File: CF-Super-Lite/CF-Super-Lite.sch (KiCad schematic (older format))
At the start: 11 parts, among them J1 Bus_ISA_8bit, J2 ATA_CONNECTOR, SW1 DIP Switch x3 or x4, U1 BIOS FLASH, U2 74HCT245, U3 GAL16V8

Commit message: Add power for CF adapter to Template and CF-Super-Lite.
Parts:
- removed J2: ATA_CONNECTOR, Connector_PinSocket_2.54mm:PinSocket_2x20_P2.54mm_Vertical, symbol 00Common:IDE_CONNECTOR
- added J1: IDE_CONNECTOR, Connector_PinSocket_2.54mm:PinSocket_2x20_P2.54mm_Vertical, symbol 00Common:IDE_CONNECTOR
- added J2: CF Adapter Power, Connector_PinHeader_2.54mm:PinHeader_1x02_P2.54mm_Vertical, symbol Connector_Generic:Conn_01x02
- renumbered J1 to J3
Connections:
- net A0: now also J1.35 (A0)
- net A1: now also J1.33 (A1)
- net A2: now also J1.36 (A2)
- net D0_BUF: now also J1.17 (D0)
- net D1_BUF: now also J1.15 (D1)
- net D2_BUF: now also J1.13 (D2)
- net D3_BUF: now also J1.11 (D3)
- net D4_BUF: now also J1.9 (D4)
- net D5_BUF: now also J1.7 (D5)
- net D6_BUF: now also J1.5 (D6)
- net D7_BUF: now also J1.3 (D7)
- net GND: now also J1.19 (GND), J1.2 (GND), J1.22 (GND), J1.24 (GND), J1.26 (GND), J1.28 (CSEL), J1.30 (GND), J1.40 (GND), J2.2 (Pin_2)
- net VCC: now also J2.1 (Pin_1)
- net ~CS0~_ATA: now also J1.37 (~CS1)
- net ~CS1~_ATA: now also J1.38 (~CS3)
- net ~IOR: now also J1.25 (~IOR)
- net ~IOW: now also J1.23 (~IOW)
- net ~RESET: now also J1.1 (~RESET)
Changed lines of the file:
@@
 	1600 3800 1100 3800
 $Comp
-L 00Common:Bus_ISA_8bit J1
+L 00Common:Bus_ISA_8bit J3
 U 1 1 6039F90B
 P 2100 2600
-F 0 "J1" H 2100 4367 50  0000 C CNN
+F 0 "J3" H 2100 4367 50  0000 C CNN
 F 1 "Bus_ISA_8bit" H 2100 4276 50  0000 C CNN
 F 2 "00Custom:BUS_XT" H 2100 2600 50  0001 C CNN
@@
 Wire Wire Line
 	1050 1400 1600 1400
-$Comp
-L 00Common:IDE_CONNECTOR J2
-U 1 1 60482C53
-P 9250 950
-F 0 "J2" H 9250 1115 50  0000 C CNN
-F 1 "ATA_CONNECTOR" H 9250 1024 50  0000 C CNN
-F 2 "Connector_PinSocket_2.54mm:PinSocket_2x20_P2.54mm_Vertical" H 9250 950 50  0001 C CNN
-F 3 "" H 9250 950 50  0001 C CNN
-	1    9250 950
-	1    0    0    -1
-$EndComp
 Text Notes 550  7700 0    50   ~ 0
 Target spec notes:\nYES Goal is to only use 3 ICs: flash rom, 245 tranceiver and GAL15V8.\nYES ROM base addresses of D800 and C800\nROM mapped in size of 16K (maybe 32 to save a pin?)\nNO Add ROM disable jumper if easy\nYES Add V20 select jumper if easy (sets a flash ROM pin high/low to use a different bank)\nNO Add activity LED header if pins available - would require two\nNO Leave out slot 8 support unless logic pins availble.
@@
 Wire Notes Line
 	9750 3250 9750 2900
+$Comp
+L 00Common:IDE_CONNECTOR J1
+U 1 1 603E717C
+P 9250 950
+F 0 "J1" H 9250 1115 50  0000 C CNN
+F 1 "IDE_CONNECTOR" H 9250 1024 50  0000 C CNN
+F 2 "Connector_PinSocket_2.54mm:PinSocket_2x20_P2.54mm_Vertical" H 9250 950 50  0001 C CNN
+F 3 "" H 9250 950 50  0001 C CNN
+	1    9250 950
+	1    0    0    -1
+$EndComp
+$Comp
+L Connector_Generic:Conn_01x02 J2
+U 1 1 603E8D26
+P 9650 4000
+F 0 "J2" H 9730 3992 50  0000 L CNN
+F 1 "CF Adapter Power" H 9730 3901 50  0000 L CNN
+F 2 "Connector_PinHeader_2.54mm:PinHeader_1x02_P2.54mm_Vertical" H 9650 4000 50  0001 C CNN
+F 3 "~" H 9650 4000 50  0001 C CNN
+	1    9650 4000
+	1    0    0    -1
+$EndComp
+$Comp
+L power:GND #PWR0123
+U 1 1 603E9698
+P 9450 4100
+F 0 "#PWR0123" H 9450 3850 50  0001 C CNN
+F 1 "GND" H 9455 3927 50  0000 C CNN
+F 2 "" H 9450 4100 50  0001 C CNN
+F 3 "" H 9450 4100 50  0001 C CNN
+	1    9450 4100
+	1    0    0    -1
+$EndComp
+$Comp
+L power:VCC #PWR0124
+U 1 1 603E9A78
+P 9450 4000
+F 0 "#PWR0124" H 9450 3850 50  0001 C CNN
+F 1 "VCC" H 9465 4173 50  0000 C CNN
+F 2 "" H 9450 4000 50  0001 C CNN
+F 3 "" H 9450 4000 50  0001 C CNN
+	1    9450 4000
+	1    0    0    -1
+$EndComp
 $EndSCHEMATC

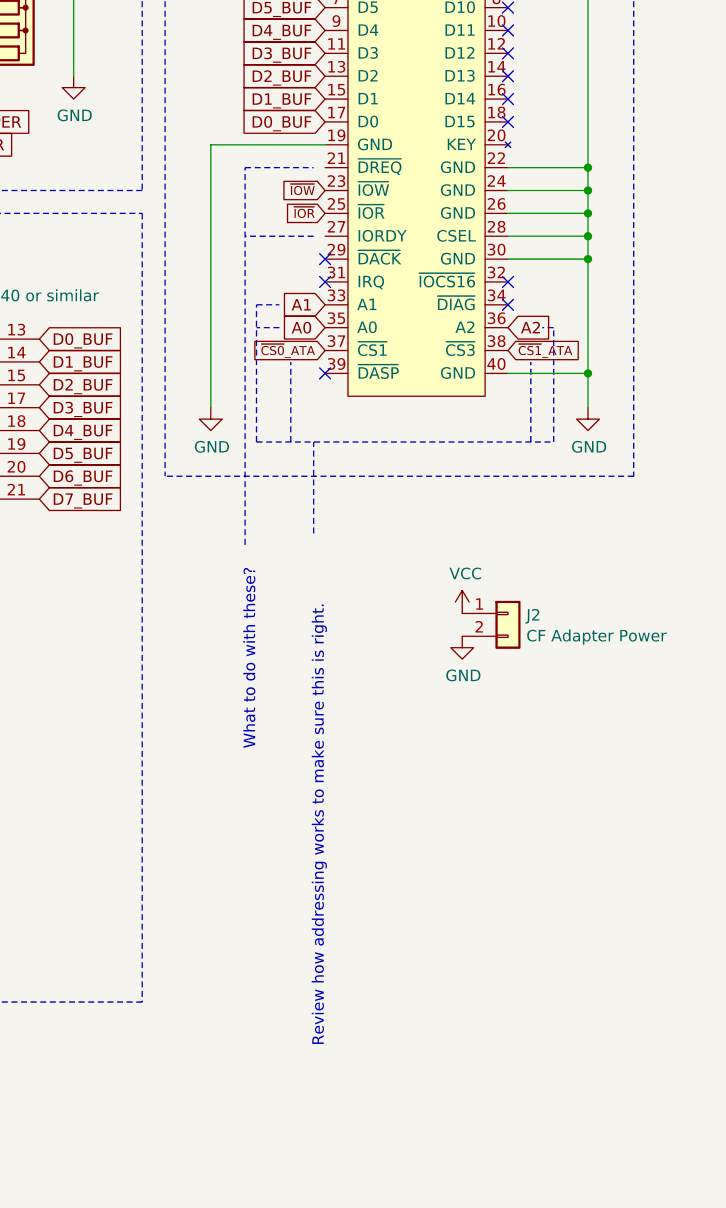
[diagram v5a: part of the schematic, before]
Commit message: Finish remaining IDE signal directions based on the ATA spec rev 1. Correct IDE address assignments and route the new connections on the PCB.
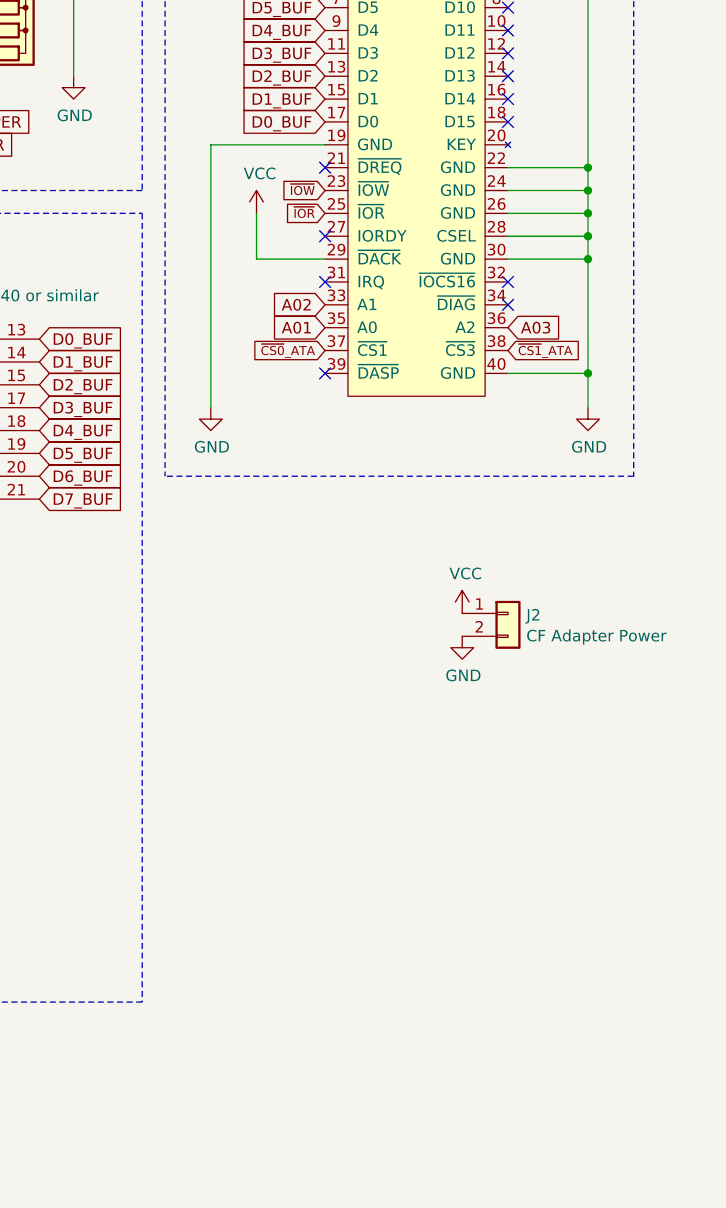
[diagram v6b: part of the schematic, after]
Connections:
- net A0 is gone; now on net A01: J1.35 (A0)
- net A1 is gone; now on net A02: J1.33 (A1)
- net A2 is gone; now on net A03: J1.36 (A2)
- net VCC: now also J1.29 (~DACK)
- no-connect marks 18 -> 19
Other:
- note removed: "Review how addressing works to make sure this is right."
- note removed: "What to do with these?"
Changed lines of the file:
@@
 NoConn ~ 9650 2650
 Text GLabel 8850 2750 0    50   Input ~ 0
-A0
+A01
 Text GLabel 8850 2650 0    50   Input ~ 0
-A1
+A02
 Text GLabel 9650 2750 2    50   Input ~ 0
-A2
+A03
 Text GLabel 9650 2850 2    39   Input ~ 0
 ~CS1~_ATA
@@
 	10000 2950 10000 3100
 NoConn ~ 8850 2550
-NoConn ~ 8850 2450
 $Comp
 L power:GND #PWR0107
@@
 Text GLabel 8850 2150 0    39   Input ~ 0
 ~IOW
-Text Notes 8550 4600 1    50   ~ 0
-What to do with these?
 Text GLabel 8850 1050 0    39   Input ~ 0
 ~RESET
@@
 Text GLabel 2700 3700 2    50   Input ~ 0
 A04
-Text Notes 8850 5900 1    50   ~ 0
-Review how addressing works to make sure this is right.
 Text GLabel 3650 1700 0    50   Input ~ 0
 A07
@@
 $EndComp
 NoConn ~ 8850 2950
-Wire Notes Line
-	8500 3700 8500 2050
-Wire Notes Line
-	8500 2050 8800 2050
-Wire Notes Line
-	8800 2350 8500 2350
-Wire Notes Line
-	8800 3650 8800 3250
-Wire Notes Line
-	9850 3250 9850 2750
-Wire Notes Line
-	9850 2750 9800 2750
-Wire Notes Line
-	8550 3250 8550 2650
-Wire Notes Line
-	8550 2650 8650 2650
-Wire Notes Line
-	8650 2750 8550 2750
-Wire Notes Line
-	8700 3250 8700 2900
-Wire Notes Line
-	8550 3250 9850 3250
-Wire Notes Line
-	9750 3250 9750 2900
 $Comp
 L 00Common:IDE_CONNECTOR J1
@@
 	1    0    0    -1
 $EndComp
+NoConn ~ 8850 2050
+NoConn ~ 8850 2350
+$Comp
+L power:VCC #PWR0125
+U 1 1 603F3CE5
+P 8550 2250
+F 0 "#PWR0125" H 8550 2100 50  0001 C CNN
+F 1 "VCC" H 8565 2423 50  0000 C CNN
+F 2 "" H 8550 2250 50  0001 C CNN
+F 3 "" H 8550 2250 50  0001 C CNN
+	1    8550 2250
+	1    0    0    -1
+$EndComp
+Wire Wire Line
+	8850 2450 8550 2450
+Wire Wire Line
+	8550 2450 8550 2250
 $EndSCHEMATC

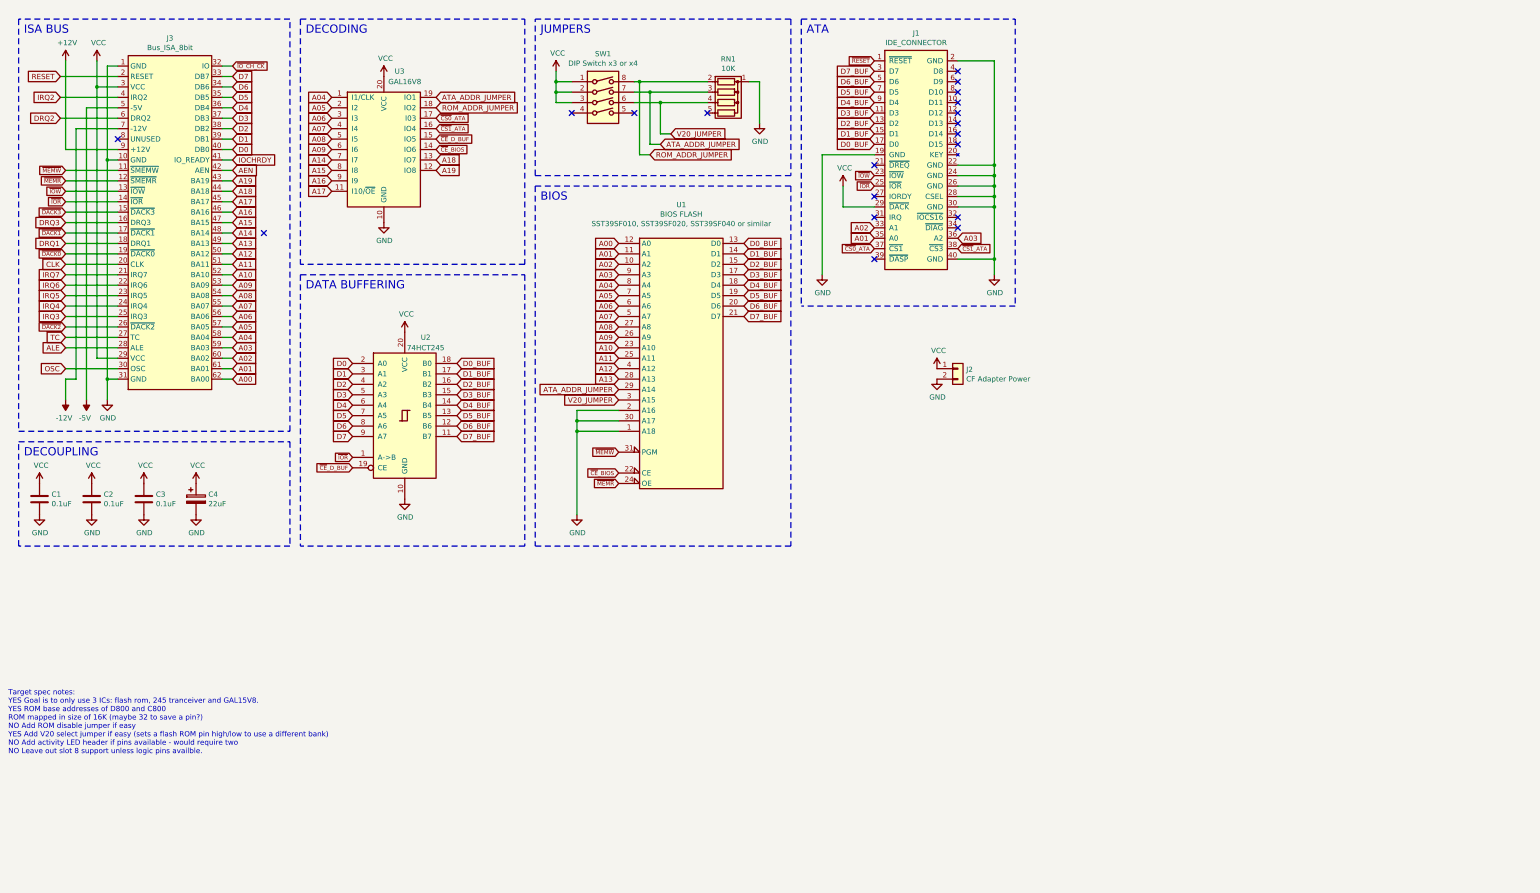
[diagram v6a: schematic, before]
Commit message: Final updates before trying to resolve unimplemented reset inversion.
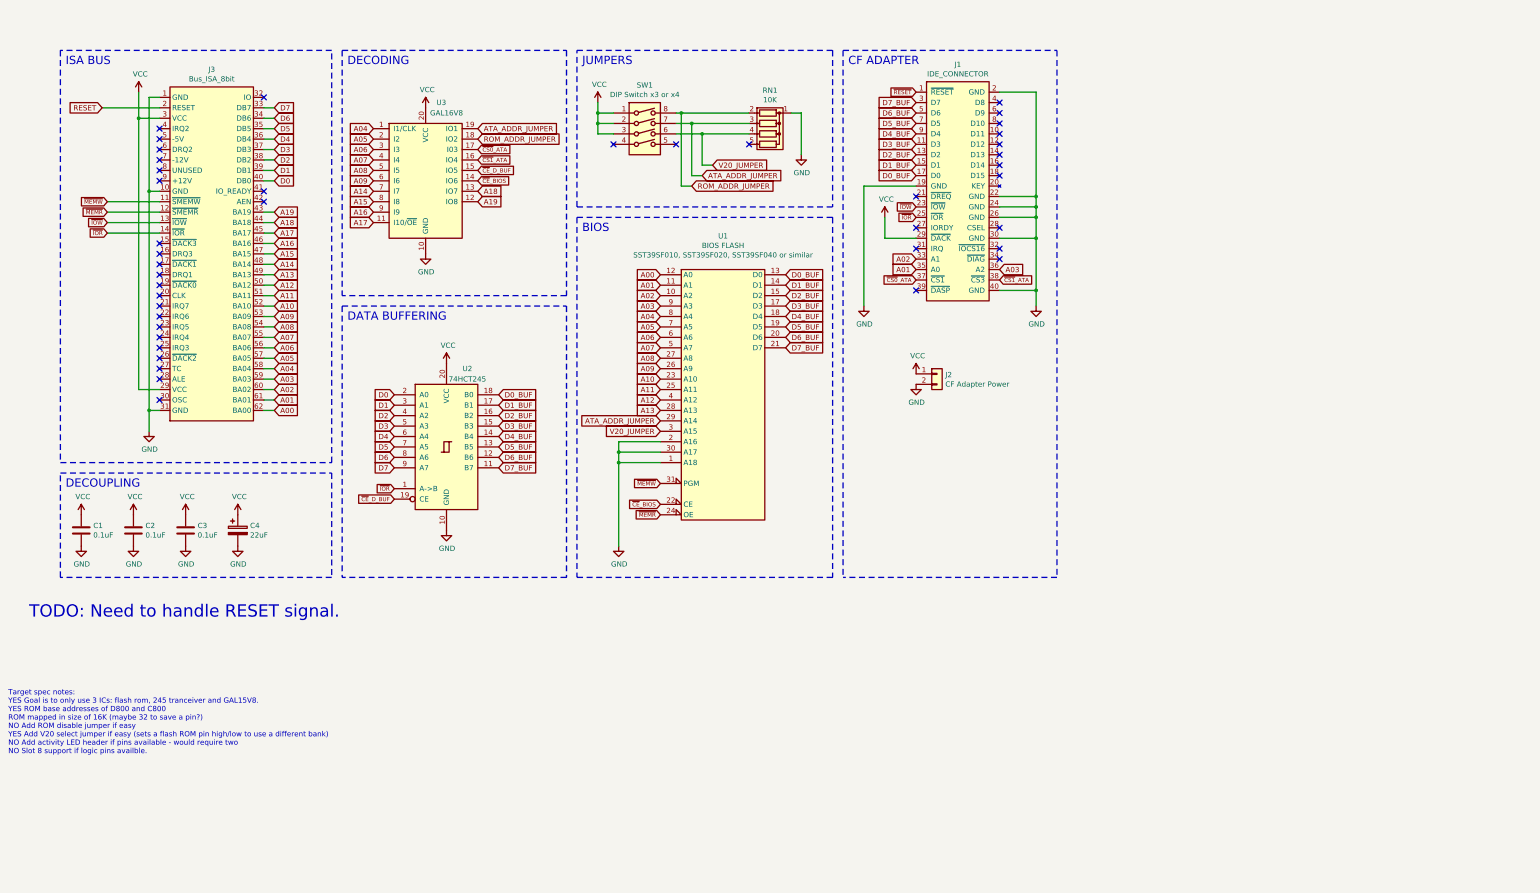
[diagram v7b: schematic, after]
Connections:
- net GND: no longer J1.28 (CSEL)
- net +12V: no longer names the net of J3.9 (+12V)
- net -12V: no longer names the net of J3.7 (-12V)
- net -5V: no longer names the net of J3.5 (-5V)
- net AEN: no longer names the net of J3.42 (AEN)
- net ALE: no longer names the net of J3.28 (ALE)
- net CLK: no longer names the net of J3.20 (CLK)
- net DRQ1: no longer names the net of J3.18 (DRQ1)
- net DRQ2: no longer names the net of J3.6 (DRQ2)
- net DRQ3: no longer names the net of J3.16 (DRQ3)
- net IOCHRDY: no longer names the net of J3.41 (IO_READY)
- net IRQ2: no longer names the net of J3.4 (IRQ2)
- net IRQ3: no longer names the net of J3.25 (IRQ3)
- net IRQ4: no longer names the net of J3.24 (IRQ4)
- net IRQ5: no longer names the net of J3.23 (IRQ5)
- net IRQ6: no longer names the net of J3.22 (IRQ6)
- net IRQ7: no longer names the net of J3.21 (IRQ7)
- net OSC: no longer names the net of J3.30 (OSC)
- net TC: no longer names the net of J3.27 (TC)
- net ~DACK0: no longer names the net of J3.19 (~DACK0)
- net ~DACK1: no longer names the net of J3.17 (~DACK1)
- net ~DACK2: no longer names the net of J3.26 (~DACK2)
- net ~DACK3: no longer names the net of J3.15 (~DACK3)
- net ~IO_CH_CK: no longer names the net of J3.32 (IO)
- no-connect marks 19 -> 42
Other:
- note added: "CF ADAPTER"
- note added: "TODO: Need to handle RESET signal."
- note added: "Target spec notes:\nYES Goal is to only use 3 ICs: flash rom, 245 tranceiver and GAL15V8.\nYES ROM base addresses of D800 and C800\nROM mapped in size of 16K (maybe 32 to save a pin?)\nNO Add ROM disable jumper if easy\nYES Add V20 select jumper if easy (sets a flash ROM pin high/low to use a different bank)\nNO Add activity LED header if pins available - would require two\nNO Slot 8 support if l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"
- note removed: "ATA"
- note removed: "Target spec notes:\nYES Goal is to only use 3 ICs: flash rom, 245 tranceiver and GAL15V8.\nYES ROM base addresses of D800 and C800\nROM mapped in size of 16K (maybe 32 to save a pin?)\nNO Add ROM disable jumper if easy\nYES Add V20 select jumper if easy (sets a flash ROM pin high/low to use a different bank)\nNO Add activity LED header if pins available - would require two\nNO Leave out slot 8 su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"
- moved on the sheet: C1, C2, C3, C4, J1, J2, J3, RN1, SW1, U1, U2, U3

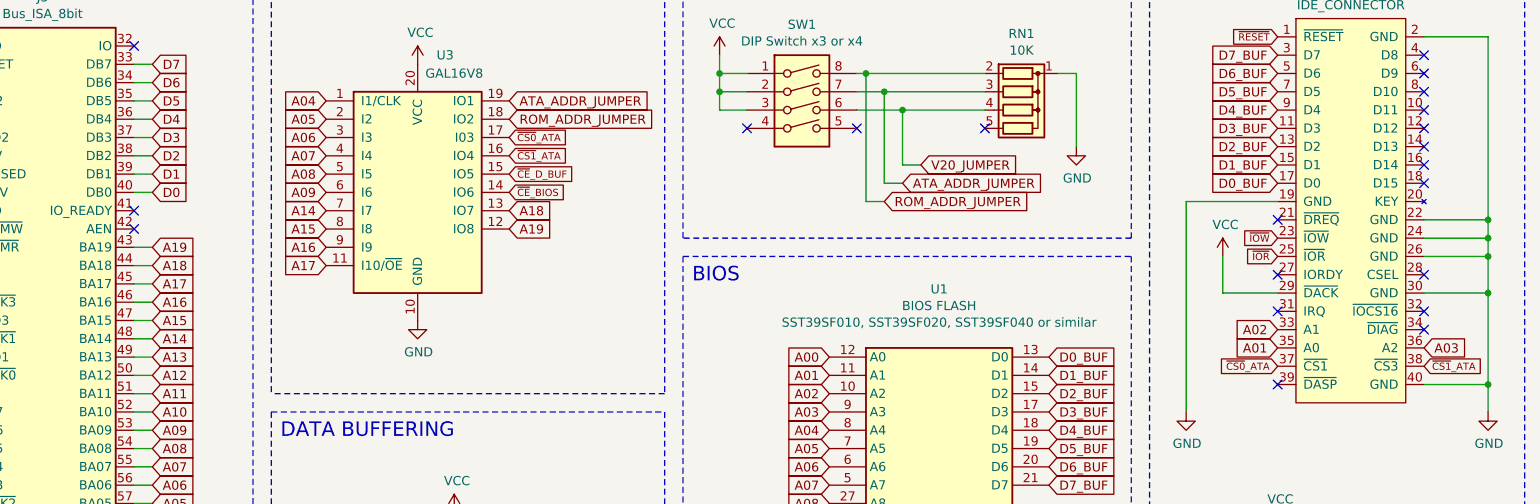
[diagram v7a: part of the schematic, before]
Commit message: Removed /CS3 output from GAL as XT-IDE doesn't seem to use it. Wemoved A14 to GAL meaning BIOS now has a 32k range in memory rather than 16k. Used freed pins to implement RESET inversion.
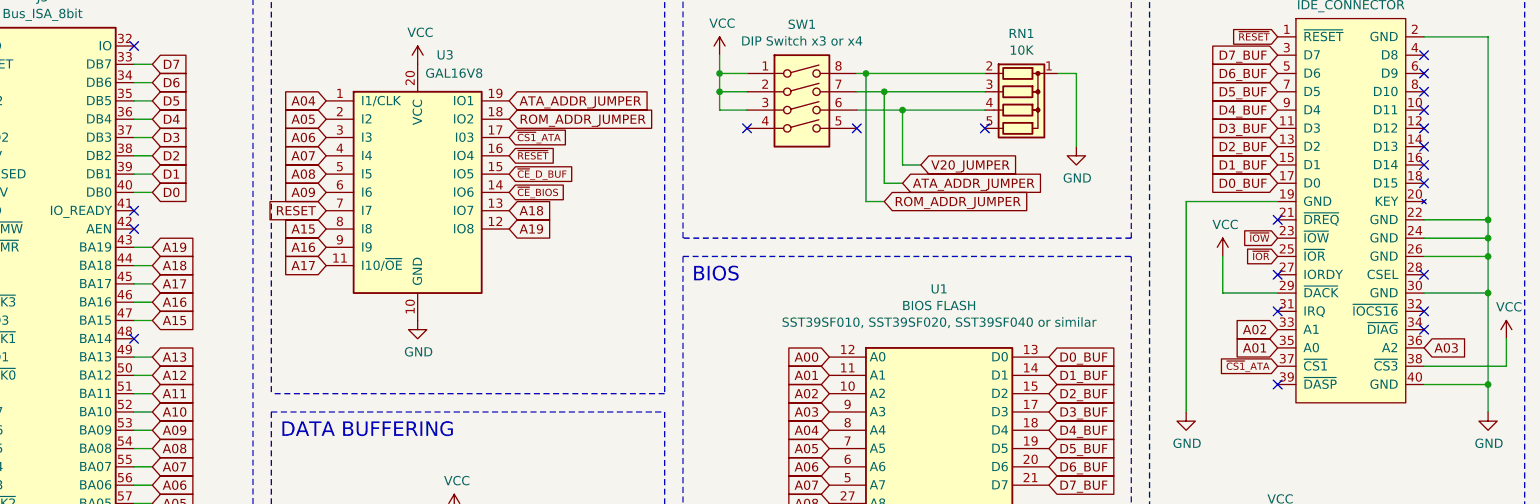
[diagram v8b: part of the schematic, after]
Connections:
- net ~CS0~_ATA is gone; now on net ~CS1~_ATA: J1.37 (~CS1), U3.17 (I03)
- net RESET: now also U3.7 (I7)
- net VCC: now also J1.38 (~CS3)
- net ~CS1~_ATA: no longer J1.38 (~CS3), U3.16 (IO4)
- net ~RESET: now also U3.16 (IO4)
- net A14: no longer names the net of J3.48 (BA14)
- net A14: no longer U3.7 (I7)
- no-connect marks 42 -> 43
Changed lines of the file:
@@
 	3000 2900 3100 2900
-Wire Wire Line
-	3000 3000 3100 3000
 Wire Wire Line
 	3000 3100 3100 3100
@@
 Text GLabel 10050 3050 2    50   Input ~ 0
 A03
-Text GLabel 10050 3150 2    39   Input ~ 0
-~CS1~_ATA
-Text GLabel 9250 3150 0    39   Input ~ 0
-~CS0~_ATA
 Wire Wire Line
 	10050 3250 10400 3250
@@
 D7_BUF
 Text GLabel 5050 1900 2    39   Input ~ 0
-~CS0~_ATA
+~CS1~_ATA
 Text GLabel 5050 2000 2    39   Input ~ 0
-~CS1~_ATA
+~RESET
 Text GLabel 5050 2200 2    39   Input ~ 0
 ~CE~_BIOS
@@
 Text GLabel 3100 2900 2    50   Input ~ 0
 A15
-Text GLabel 3100 3000 2    50   Input ~ 0
-A14
 Text GLabel 5050 2400 2    50   Input ~ 0
 A19
@@
 Text GLabel 4050 2400 0    50   Input ~ 0
 A15
-Text GLabel 4050 2300 0    50   Input ~ 0
-A14
 Text GLabel 5050 1800 2    50   Input ~ 0
 ROM_ADDR_JUMPER
@@
 Text Notes 750  6400 0    118  ~ 0
 TODO: Need to handle RESET signal.
+Text GLabel 4050 2300 0    50   Input ~ 0
+RESET
+Wire Wire Line
+	10050 3150 10500 3150
+Wire Wire Line
+	10500 3150 10500 3000
+$Comp
+L power:VCC #PWR0103
+U 1 1 60476F5F
+P 10500 3000
+F 0 "#PWR0103" H 10500 2850 50  0001 C CNN
+F 1 "VCC" H 10515 3173 50  0000 C CNN
+F 2 "" H 10500 3000 50  0001 C CNN
+F 3 "" H 10500 3000 50  0001 C CNN
+	1    10500 3000
+	1    0    0    -1
+$EndComp
+Text GLabel 9250 3150 0    39   Input ~ 0
+~CS1~_ATA
+NoConn ~ 3000 3000
 $EndSCHEMATC
